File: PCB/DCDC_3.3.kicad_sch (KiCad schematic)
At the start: 18 parts, among them U11 LV2842XLVDDCR

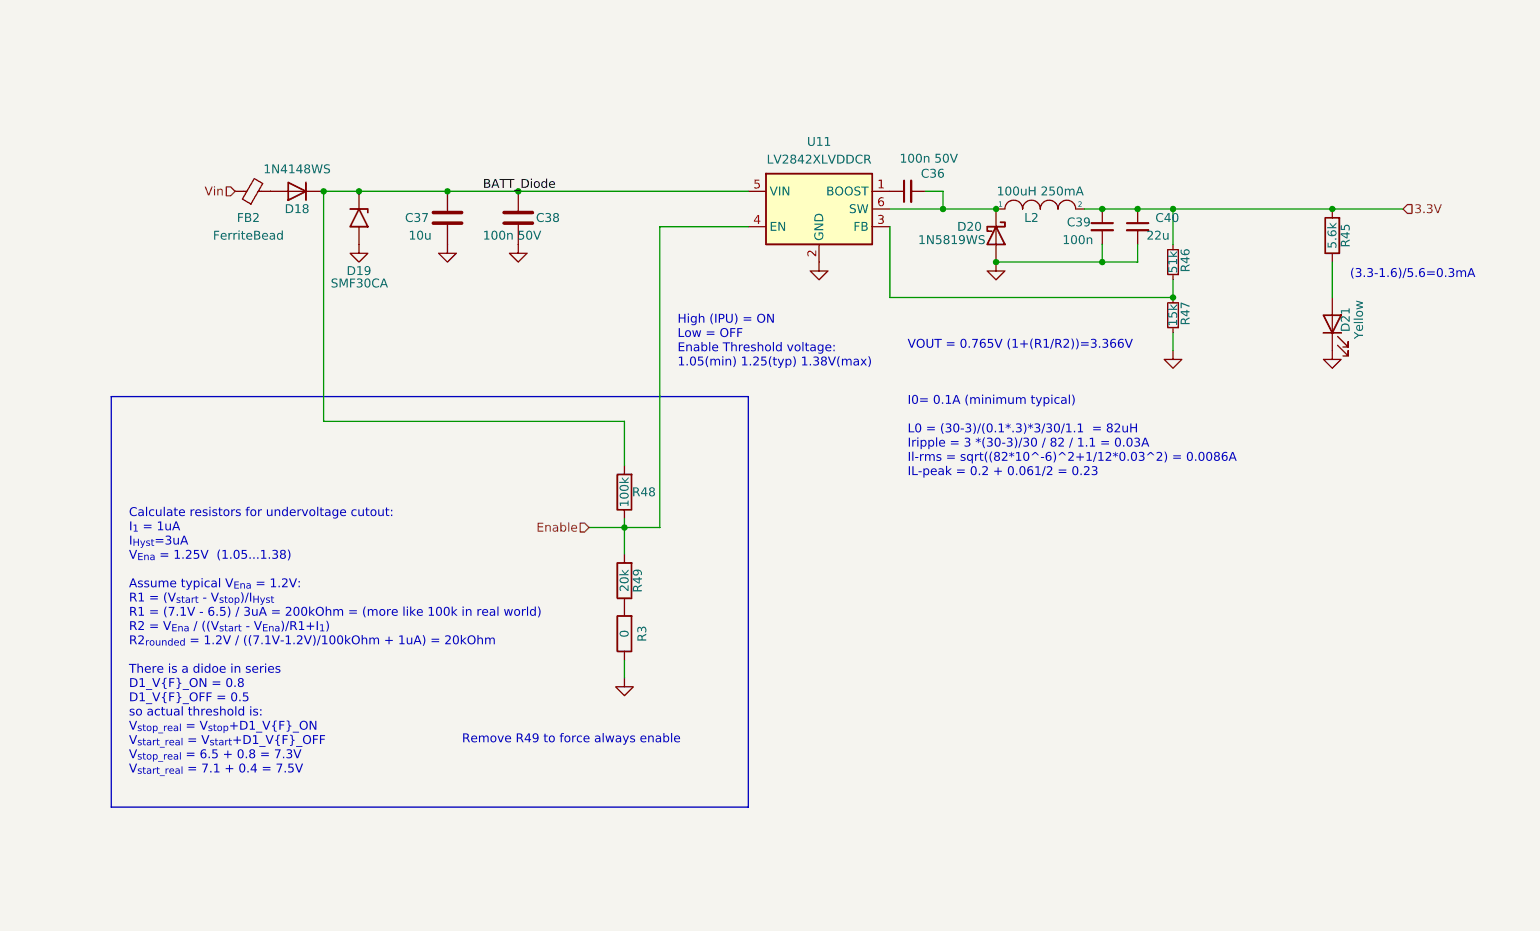
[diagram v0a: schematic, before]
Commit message: Removed input ferrite bead
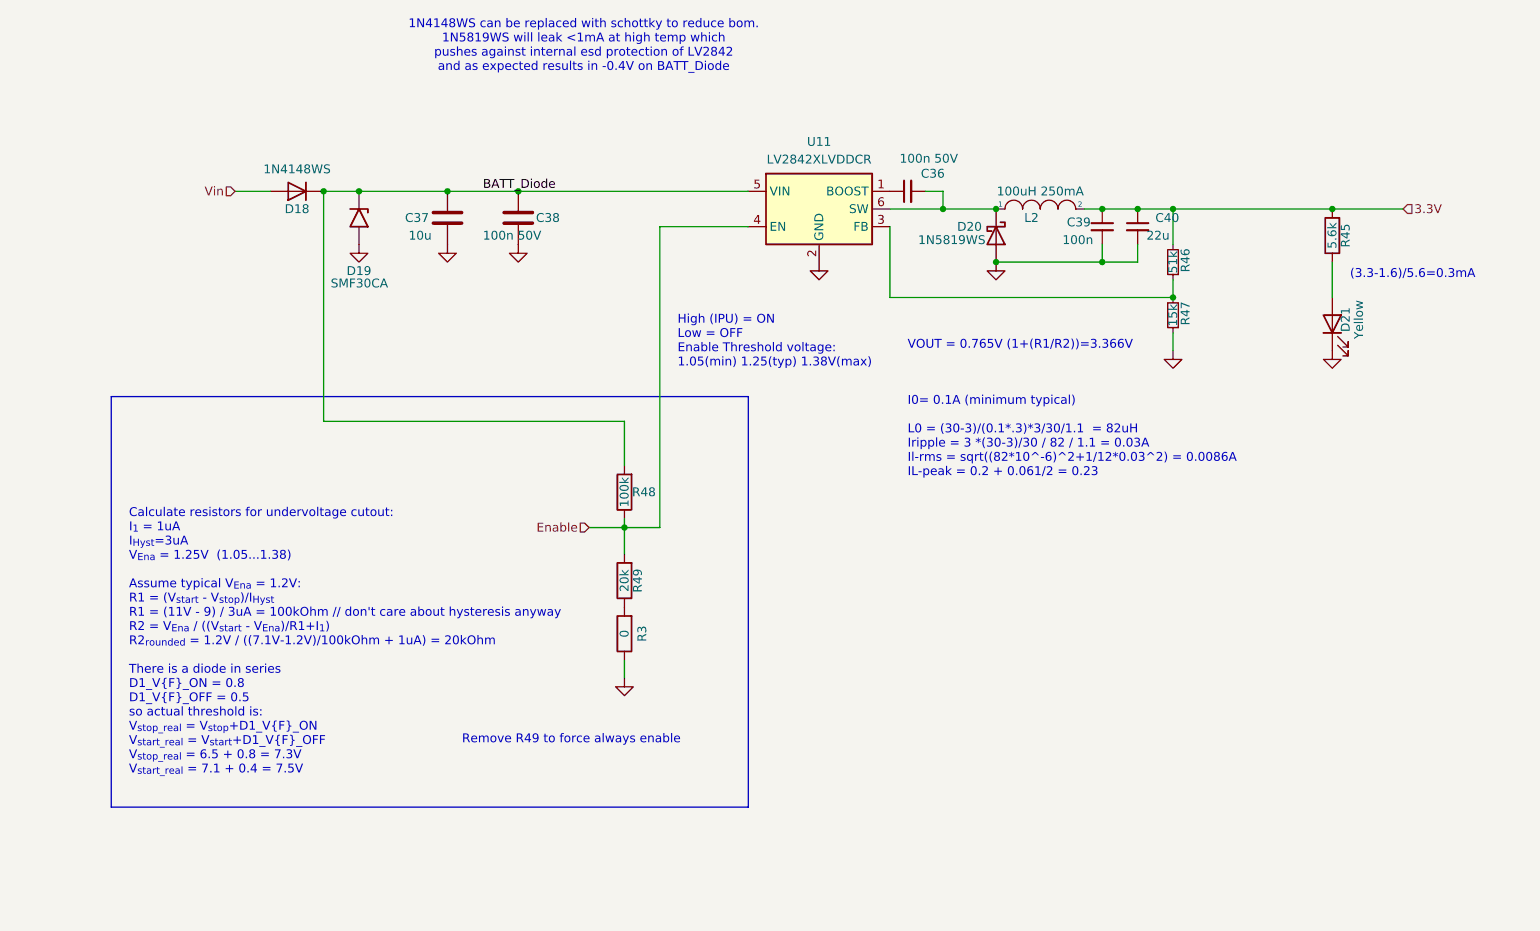
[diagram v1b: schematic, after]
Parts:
- removed FB2: FerriteBead, Inductor_SMD:L_0603_1608Metric, symbol Device:FerriteBead_Small
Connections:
- net Vin: now also D18.2 (A)
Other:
- note added: "1N4148WS can be replaced with schottky to reduce bom. 1N5819WS will leak <1mA at high temp which pushes against internal esd protection of LV2842 and as expected results in -0.4V on BATT_Diode"
- note added: "Calculate resistors for undervoltage cutout: I_{1} = 1uA I_{Hyst}=3uA V_{Ena} = 1.25V (1.05...1.38) Assume typical V_{Ena} = 1.2V: R1 = (V_{start} - V_{stop})/I_{Hyst} R1 = (11V - 9) / 3uA = 100kOhm // don't care about hysteresis anyway R2 = V_{Ena} / ((V_{start} - V_{Ena})/R1+I_{1}) R2_{rounded} = 1.2V / ((7.1V-1.2V)/100kOhm + 1uA) = 20kOhm There is a diode in series D1_V{F}_ON = 0.8 D1_V{F}_OFF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"
- note removed: "Calculate resistors for undervoltage cutout: I_{1} = 1uA I_{Hyst}=3uA V_{Ena} = 1.25V (1.05...1.38) Assume typical V_{Ena} = 1.2V: R1 = (V_{start} - V_{stop})/I_{Hyst} R1 = (7.1V - 6.5) / 3uA = 200kOhm = (more like 100k in real world) R2 = V_{Ena} / ((V_{start} - V_{Ena})/R1+I_{1}) R2_{rounded} = 1.2V / ((7.1V-1.2V)/100kOhm + 1uA) = 20kOhm There is a didoe in series D1_V{F}_ON = 0.8 D1_V{F}_OFF =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"
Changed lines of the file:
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@@
 		)
 	)
-	(text "Calculate resistors for undervoltage cutout:\nI_{1} = 1uA\nI_{Hyst}=3uA\nV_{Ena} = 1.25V  (1.05...1.38)\n\nAssume typical V_{Ena} = 1.2V:\nR1 = (V_{start} - V_{stop})/I_{Hyst}\nR1 = (7.1V - 6.5) / 3uA = 200kOhm = (more like 100k in real world)\nR2 = V_{Ena} / ((V_{start} - V_{Ena})/R1+I_{1})\nR2_{rounded} = 1.2V / ((7.1V-1.2V)/100kOhm + 1uA) = 20kOhm\n\nThere is a didoe in series\nD1_V{F}_ON = 0.8\nD1_V{F}_OFF = 0.5\nso actual threshold is:\nV_{stop_real} = V_{stop}+D1_V{F}_ON\nV_{start_real} = V_{start}+D1_V{F}_OFF\nV_{stop_real} = 6.5 + 0.8 = 7.3V\nV_{start_real} = 7.1 + 0.4 = 7.5V"
+	(text "1N4148WS can be replaced with schottky to reduce bom.  \n1N5819WS will leak <1mA at high temp which \npushes against internal esd protection of LV2842 \nand as expected results in -0.4V on BATT_Diode"
+		(exclude_from_sim no)
+		(at 103.378 60.452 0)
+		(effects
+			(font
+				(size 1.27 1.27)
+			)
+		)
+	)
+	(text "Calculate resistors for undervoltage cutout:\nI_{1} = 1uA\nI_{Hyst}=3uA\nV_{Ena} = 1.25V  (1.05...1.38)\n\nAssume typical V_{Ena} = 1.2V:\nR1 = (V_{start} - V_{stop})/I_{Hyst}\nR1 = (11V - 9) / 3uA = 100kOhm // don't care about hysteresis anyway\nR2 = V_{Ena} / ((V_{start} - V_{Ena})/R1+I_{1})\nR2_{rounded} = 1.2V / ((7.1V-1.2V)/100kOhm + 1uA) = 20kOhm\n\nThere is a diode in series\nD1_V{F}_ON = 0.8\nD1_V{F}_OFF = 0.5\nso actual threshold is:\nV_{stop_real} = V_{stop}+D1_V{F}_ON\nV_{start_real} = V_{start}+D1_V{F}_OFF\nV_{stop_real} = 6.5 + 0.8 = 7.3V\nV_{start_real} = 7.1 + 0.4 = 7.5V"
 		(exclude_from_sim no)
 		(at 38.1 165.1 0)
@@
 		(pts
 			(xy 187.96 83.82) (xy 210.82 83.82)
+		)
+		(stroke
+			(width 0)
+			(type default)
+		)
+	)
+	(wire
+		(pts
+			(xy 53.34 81.28) (xy 58.42 81.28)
 		)
 		(stroke
@@
 					(unit 1)
 				)
-			)
-		)
-	)
-	(symbol
-		(lib_id "Device:FerriteBead_Small")
-		(at 55.88 81.28 90)
-		(unit 1)
-		(exclude_from_sim no)
-		(in_bom yes)
-		(on_board yes)
-		(dnp no)
-		(property "Reference" "FB2"
-			(at 55.245 85.09 90)
-			(effects
-				(font
-					(size 1.27 1.27)
-				)
-			)
-		)
-		(property "Value" "FerriteBead"
-			(at 55.245 87.63 90)
-			(effects
-				(font
-					(size 1.27 1.27)
-				)
-			)
-		)
-		(property "Footprint" "Inductor_SMD:L_0603_1608Metric"
-			(at 55.88 83.058 90)
-			(effects
-				(font
-					(size 1.27 1.27)
-				)
-				(hide yes)
-			)
-		)
-		(property "Datasheet" "https://datasheet.lcsc.com/lcsc/2109180930_Sunlord-GZ1608D601TF_C1002.pdf"
-			(at 55.88 81.28 0)
-			(effects
-				(font
-					(size 1.27 1.27)
-				)
-				(hide yes)
-			)
-		)
-		(property "Description" "This one is 200mA which is way above the limit because at 12V current is 4x smaller"
-			(at 55.88 81.28 90)
-			(effects
-				(font
-					(size 1.27 1.27)
-				)
-				(hide yes)
-			)
-		)
-		(property "LCSC" "C1002"
-			(at 55.88 81.28 90)
-			(effects
-				(font
-					(size 1.27 1.27)
-				)
-				(hide yes)
-			)
-		)
-		(pin "1"
-		)
-		(pin "2"
-		)
-		(instances
-			(project "StepperServoCAN"
-				(path "/92dad13e-412a-43d4-9260-9087579302b1/82f027ad-2d00-453d-ab1c-0ba3b5cb1ef7"
-					(reference "FB2")
-					(unit 1)
-				)

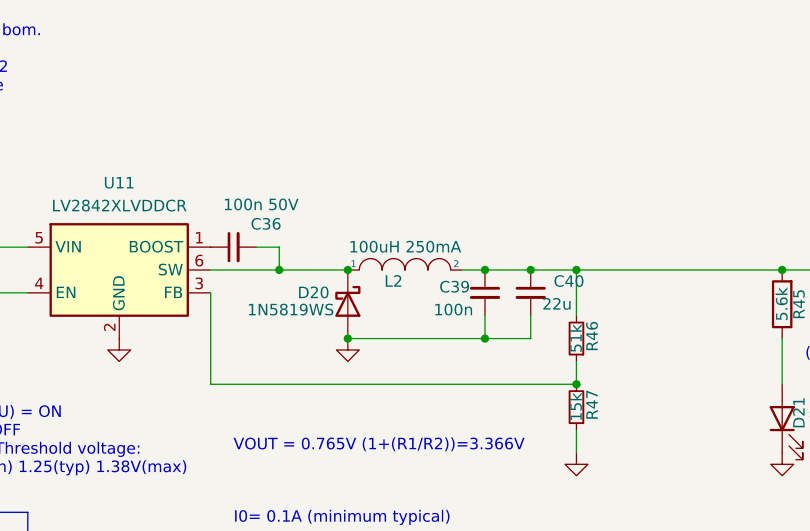
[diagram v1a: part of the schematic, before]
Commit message: Better Wire Wound Molded SMD Power Inductor
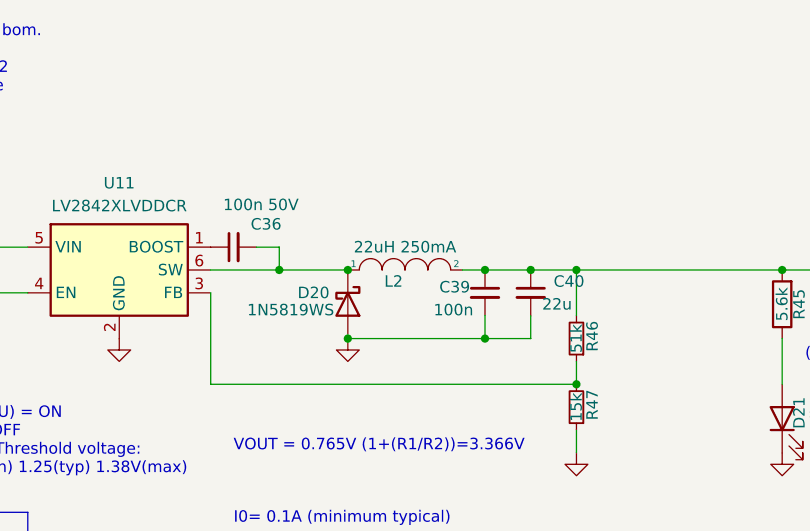
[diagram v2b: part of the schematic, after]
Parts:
- L2: value 100uH 250mA -> 22uH 250mA; footprint Inductor_SMD:L_Sunlord_SWPA3012S -> Inductor_SMD:L_Cenker_CKCS252010; LCSC C167741 -> C5832391
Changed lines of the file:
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@@
 			)
 		)
-		(property "Value" "100uH 250mA"
+		(property "Value" "22uH 250mA"
 			(at 168.91 81.28 0)
 			(effects
@@
 			)
 		)
-		(property "Footprint" "Inductor_SMD:L_Sunlord_SWPA3012S"
+		(property "Footprint" "Inductor_SMD:L_Cenker_CKCS252010"
 			(at 168.91 83.82 0)
 			(effects
@@
 			)
 		)
-		(property "Datasheet" "https://datasheet.lcsc.com/lcsc/1810061014_cjiang-Changjiang-Microelectronics-Tech-FNR4030S221MT_C167899.pdf"
+		(property "Datasheet" "https://jlcpcb.com/api/file/downloadByFileSystemAccessId/8590903698845884416"
 			(at 168.91 83.82 0)
 			(effects
@@
 			)
 		)
-		(property "LCSC" "C167741"
+		(property "LCSC" "C5832391"
 			(at 168.91 83.82 0)
 			(effects

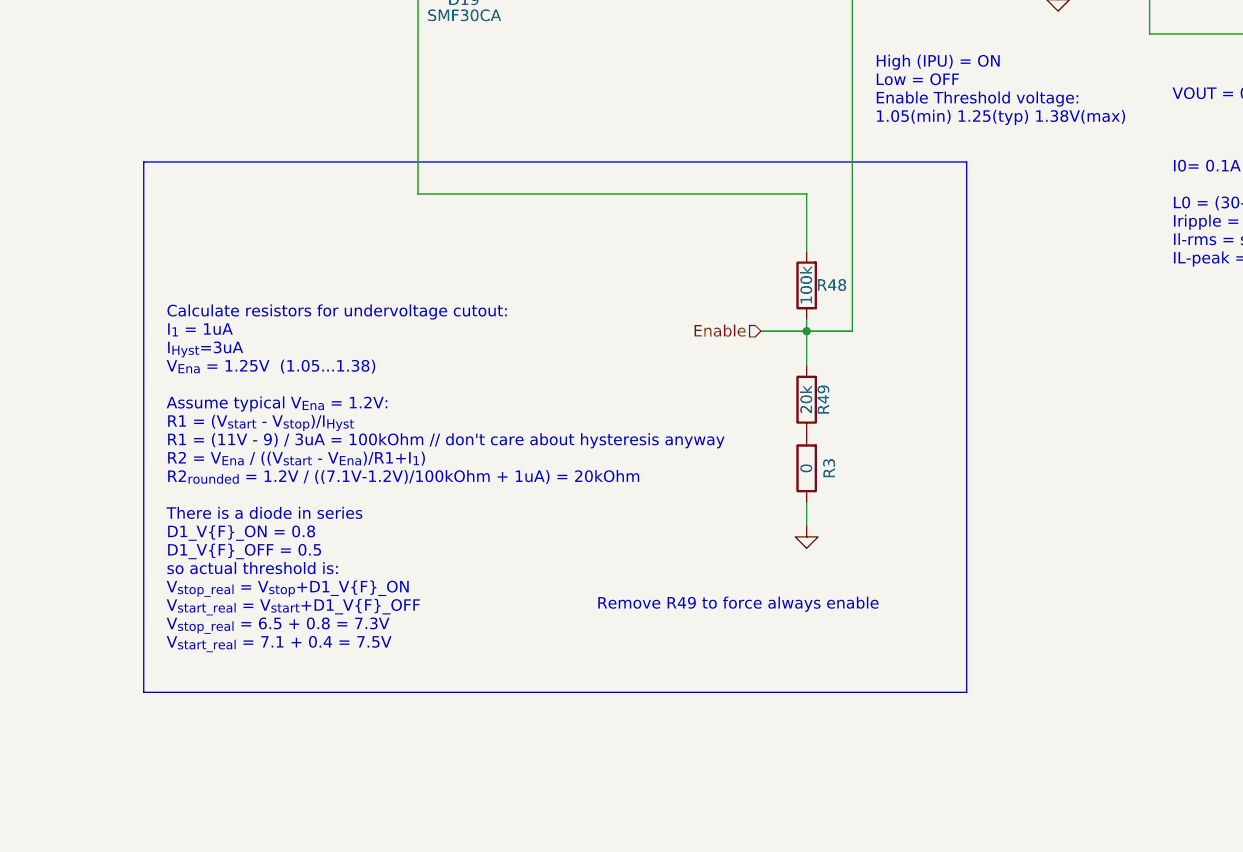
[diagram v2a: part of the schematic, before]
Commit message: Min voltage 12V.  DCDC shutdown from gpio via mosfet. Large hysteresis using 3.3V feedback resistor to avoid immediate restart if lower than 12V supply.
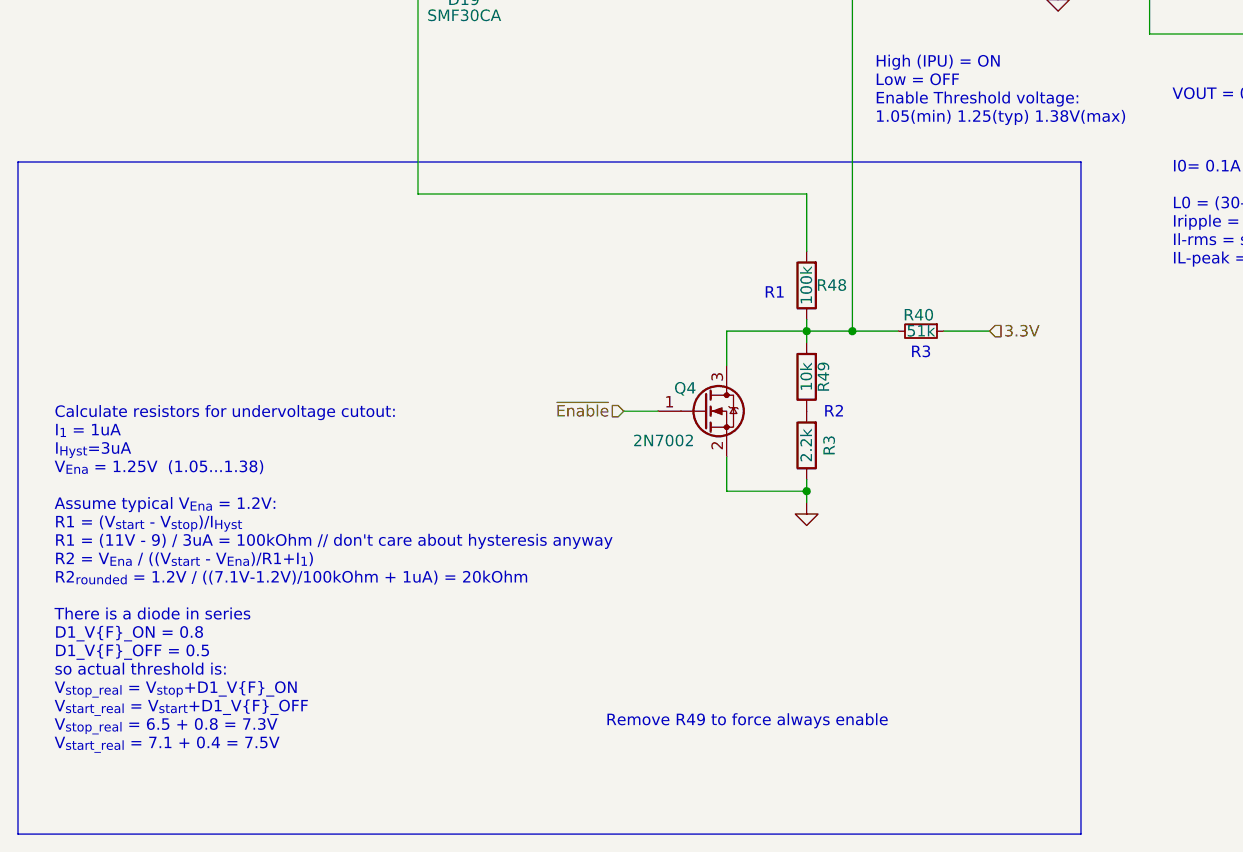
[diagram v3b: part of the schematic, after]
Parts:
- added Q4: 2N7002, Package_TO_SOT_SMD:SOT-23, symbol Transistor_FET:2N7002
- added R40: 51k, Resistor_SMD:R_0402_1005Metric, symbol Device:R_Small
- R3: value 0 -> 2.2k; LCSC (none) -> C25879
- R49: value 20k -> 10k; LCSC C25765 -> C25744
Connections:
- net 3.3V: now also R40.1
- net GND: now also Q4.2 (S)
- net Enable: no longer names the net of R48.1, R49.2, U11.4 (EN)
- net Enable: now also Q4.3 (D), R40.2
- new net ~{Enable}: Q4.1 (G)
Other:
- note added: "R1"
- note added: "R2"
- note added: "R3"
- moved on the sheet: R3, R49

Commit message: parts availability
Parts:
- D19: LCSC C2990493 -> C19077519
- D21: LCSC C72038 -> C89811
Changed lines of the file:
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@@
 			)
 		)
-		(property "LCSC" "C2990493"
+		(property "LCSC" "C19077519"
 			(at 71.12 85.09 0)
 			(effects
@@
 			)
 		)
-		(property "LCSC" "C72038"
+		(property "LCSC" "C89811"
 			(at 212.725 99.695 0)
 			(effects
